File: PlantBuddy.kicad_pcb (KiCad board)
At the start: 4 copper layers, 35 x 35 mm, 67 parts, among them J1 USB_C_Receptacle_USB2.0, J102 Debug, J2 Conn_Coaxial, J4 External, SW1 SW_Push, U1 LTR-303ALS-01, U102 nRF52832-QFAA, U106 CP2102N-Axx-xQFN20, U2 SHTC3, U3 XC6206PxxxMR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

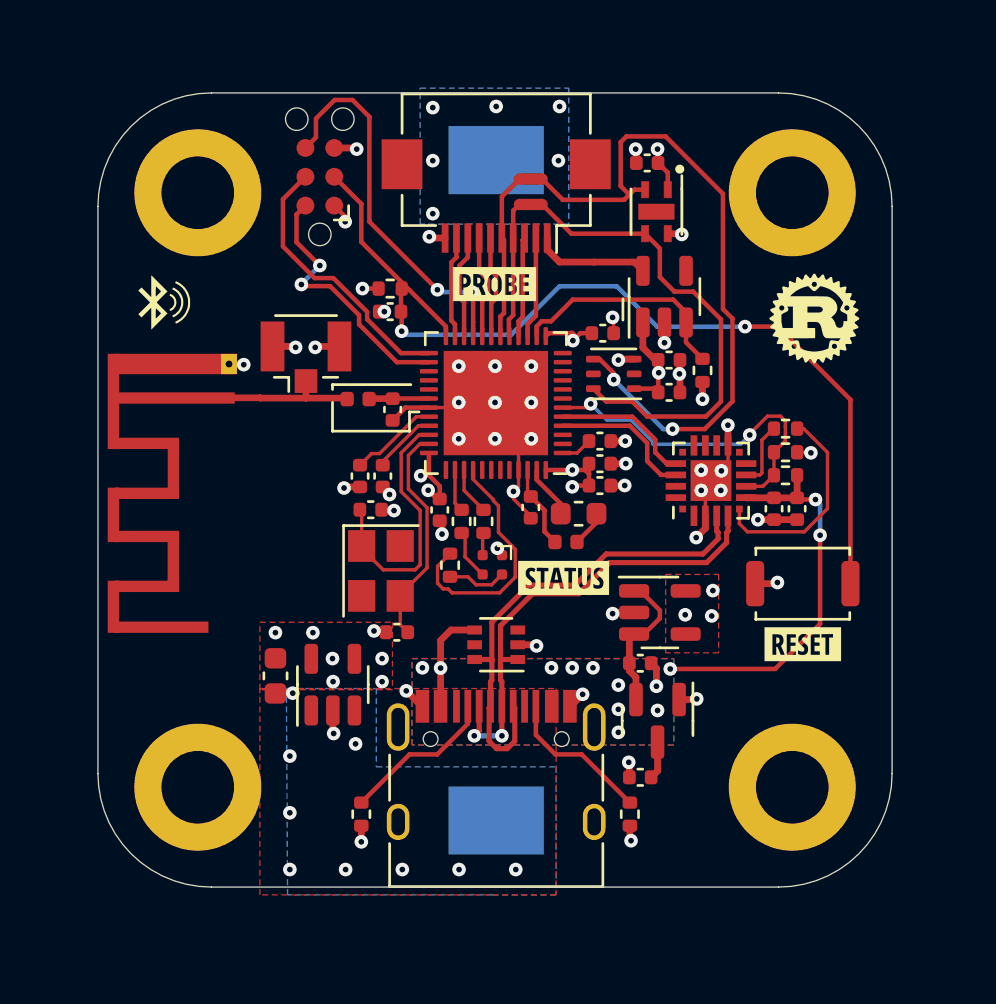
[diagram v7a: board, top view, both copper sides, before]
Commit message: PCB changes after testing.
- separated i2c buses
- changed layer stackup to sig-gnd-gnd-sig
- added top & bottom ground layers
- routed power on bottom layer
- added LF crystal
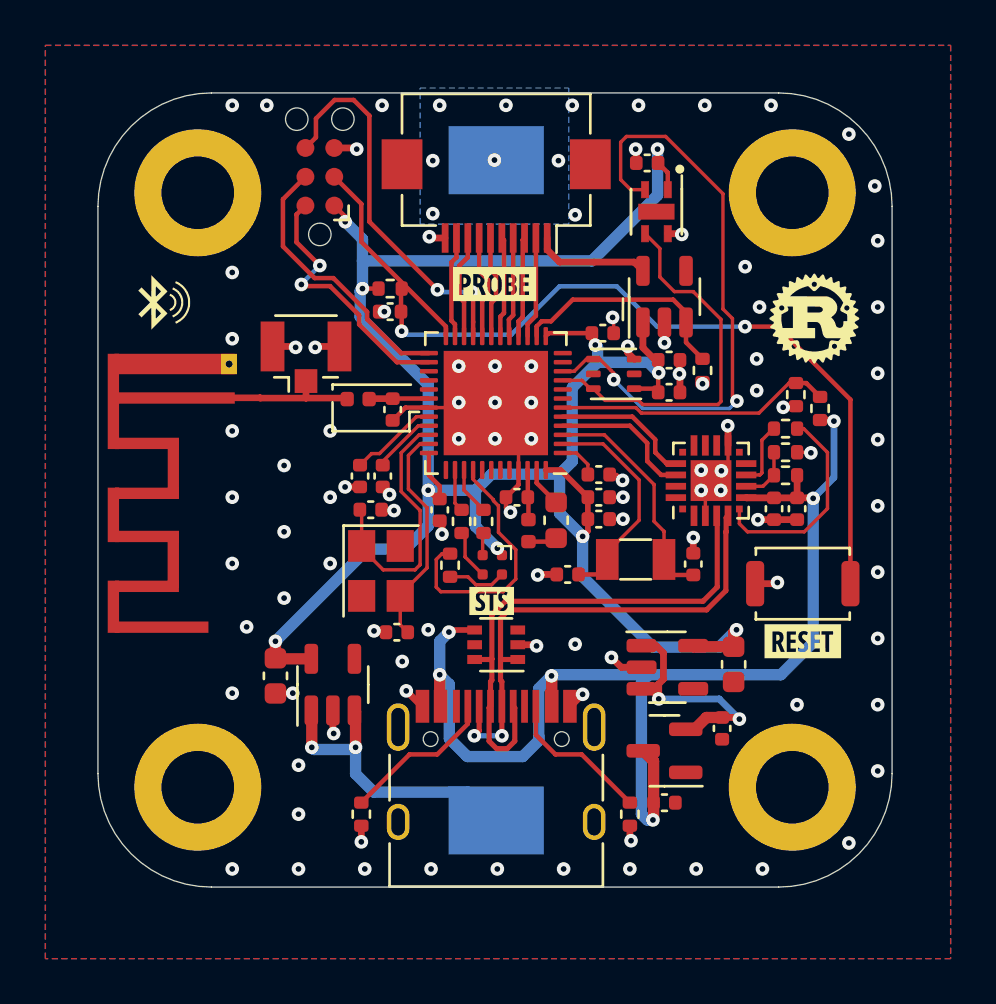
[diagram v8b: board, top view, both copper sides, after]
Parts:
- removed NT101, NT102: NetTie_2, NetTie:NetTie-2_SMD_Pad0.5mm
- added C7: 15pF, Capacitor_SMD:C_0402_1005Metric, F.Cu at (126.2, 70.8)
- added C8: 15pF, Capacitor_SMD:C_0402_1005Metric, F.Cu at (120.7, 71.2)
- added C9: 22uF, Capacitor_SMD:C_0603_1608Metric, F.Cu at (128.0, 75.2)
- added R3: 22k, Resistor_SMD:R_0402_1005Metric, F.Cu at (131.8, 63.9)
- added R4: 22k, Resistor_SMD:R_0402_1005Metric, F.Cu at (130.8, 63.3)
- added Y1: 32kHz, Crystal:Crystal_SMD_3215-2Pin_3.2x1.5mm, F.Cu at (123.7, 70.6)
- R106: value 22k -> 47k
- moved C4 4.61 mm to (127.5, 78.0), turned to -90 degrees
- moved G*** 3.33 mm to (117.3, 72.4)
- moved C112 2.44 mm to (122.1, 68.8)
- moved U6 2.44 mm to (125.1, 75.3)
- moved L103 1.73 mm to (119.0, 69.3), turned to -90 degrees
- moved C3 1.55 mm to (125.0, 81.3), turned to 0 degrees
- moved C117 1.47 mm to (122.1, 66.8)
- moved U3 1.36 mm to (125.0, 79.0), turned to 180 degrees
- moved L102 1.03 mm to (120.2, 68.8), turned to 90 degrees
- moved C111 0.76 mm to (118.5, 67.8), turned to 180 degrees
- moved C114 0.52 mm to (122.1, 67.8)
- moved G*** 0.13 mm to (131.1, 74.2)
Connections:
- J1 pad S1: GND -> unconnected-(J1-PadS1)
- R104 pad 2: /USBDet -> Net-(R104-Pad2)
- R106 pad 1: /USBDet -> Net-(R104-Pad2)
- U102 pad 10: unconnected-(U102-Pad10) -> /SCL
- U102 pad 2: unconnected-(U102-Pad2) -> Net-(U102-Pad2)
- U102 pad 3: unconnected-(U102-Pad3) -> Net-(U102-Pad3)
- U102 pad 9: unconnected-(U102-Pad9) -> /SDA
- U106 pad 8: /USBDet -> Net-(R104-Pad2)
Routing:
- net +3V0: track 18.1 -> 95.0 mm, vias 19 -> 10
- net VBUS: track 23.3 -> 53.5 mm, vias 12 -> 6
- net /bat+: track 0.00 -> 13.5 mm, vias 8 -> 2
- net Net-(U102-Pad2): track 0.00 -> 10.4 mm
- net Net-(U102-Pad3): track 0.00 -> 10.4 mm
- net +3.3V: track 6.36 -> 10.6 mm, vias 0 -> 2
- net /SDA: track 20.7 -> 16.7 mm
- net /SCL: track 30.7 -> 27.1 mm
- net /USBDet: track 15.3 -> 12.2 mm, vias 2 -> 0
- net GND: track 42.4 -> 39.5 mm, vias 57 -> 107
- net /EXT4: track 7.35 -> 4.43 mm
- net Net-(R104-Pad2): track 0.00 -> 2.44 mm
- net /EXT3: track 6.01 -> 4.41 mm
- net /DEC4: track 3.67 -> 2.20 mm
- net /D-: track 20.9 -> 22.4 mm
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- added copper zone on F.Cu, net GND
- added copper zone on In2.Cu, net GND
- removed copper zone on F.Cu, net +3V0
- removed copper zone on In2.Cu, net +3V0
- removed copper zone on B.Cu, net /bat+
- removed copper zone on F.Cu, net /bat+
- removed copper zone on B.Cu, net VBUS
- removed copper zone on F.Cu, net VBUS
